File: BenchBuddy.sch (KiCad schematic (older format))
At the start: 0 parts

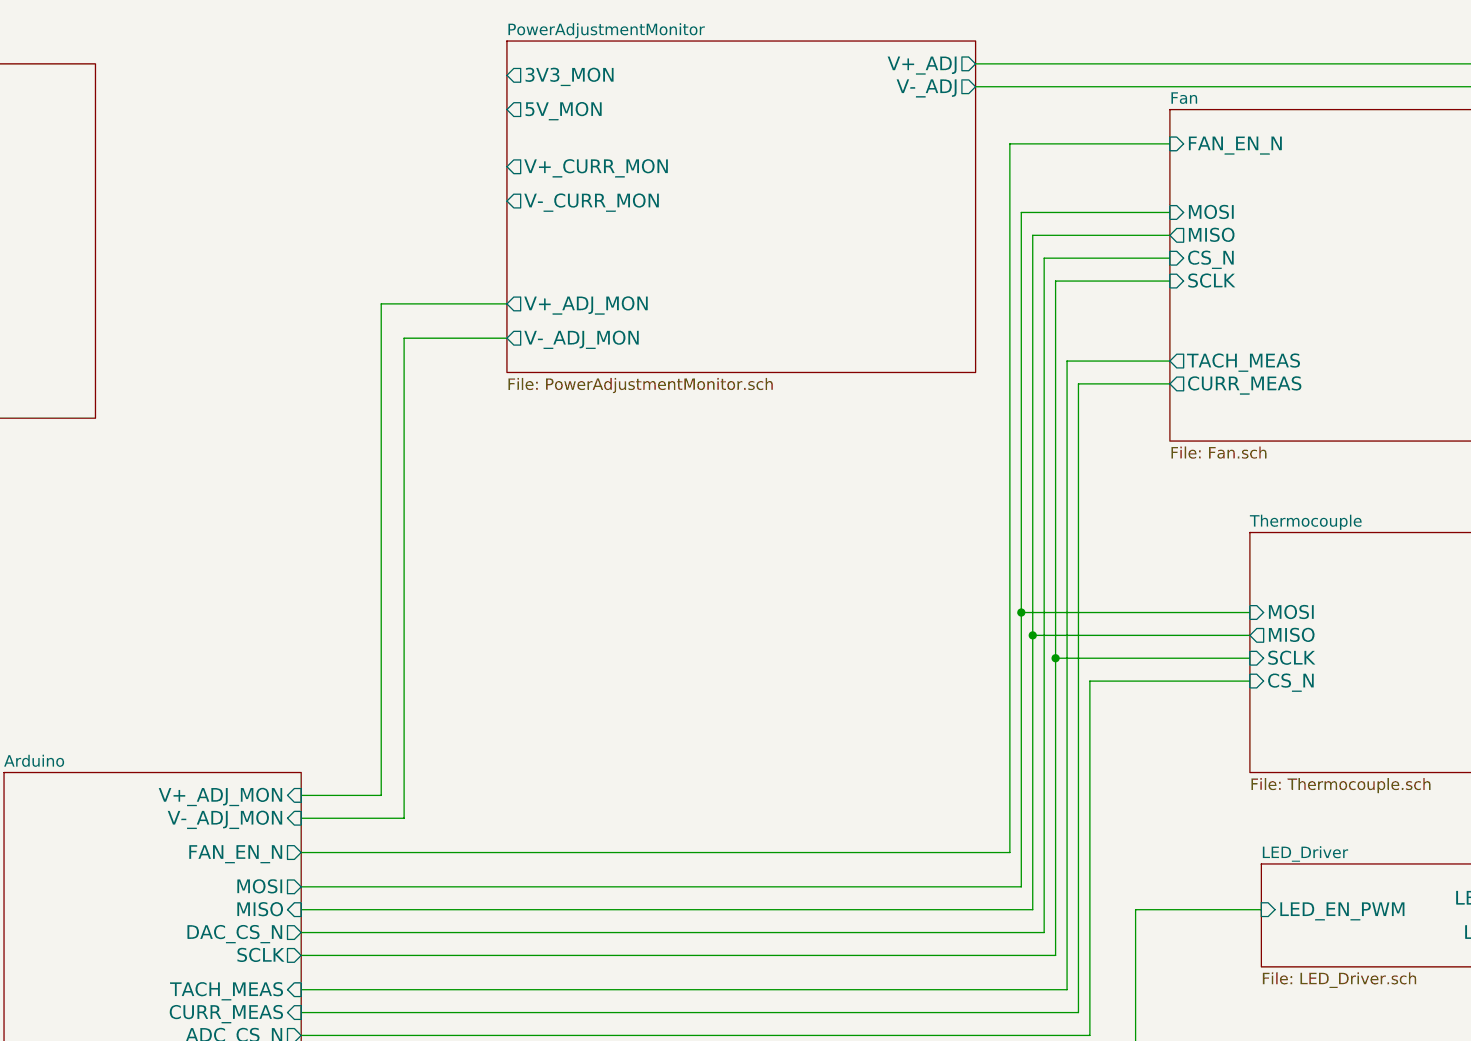
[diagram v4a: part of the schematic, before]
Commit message: Fan/Current Module Refactoring
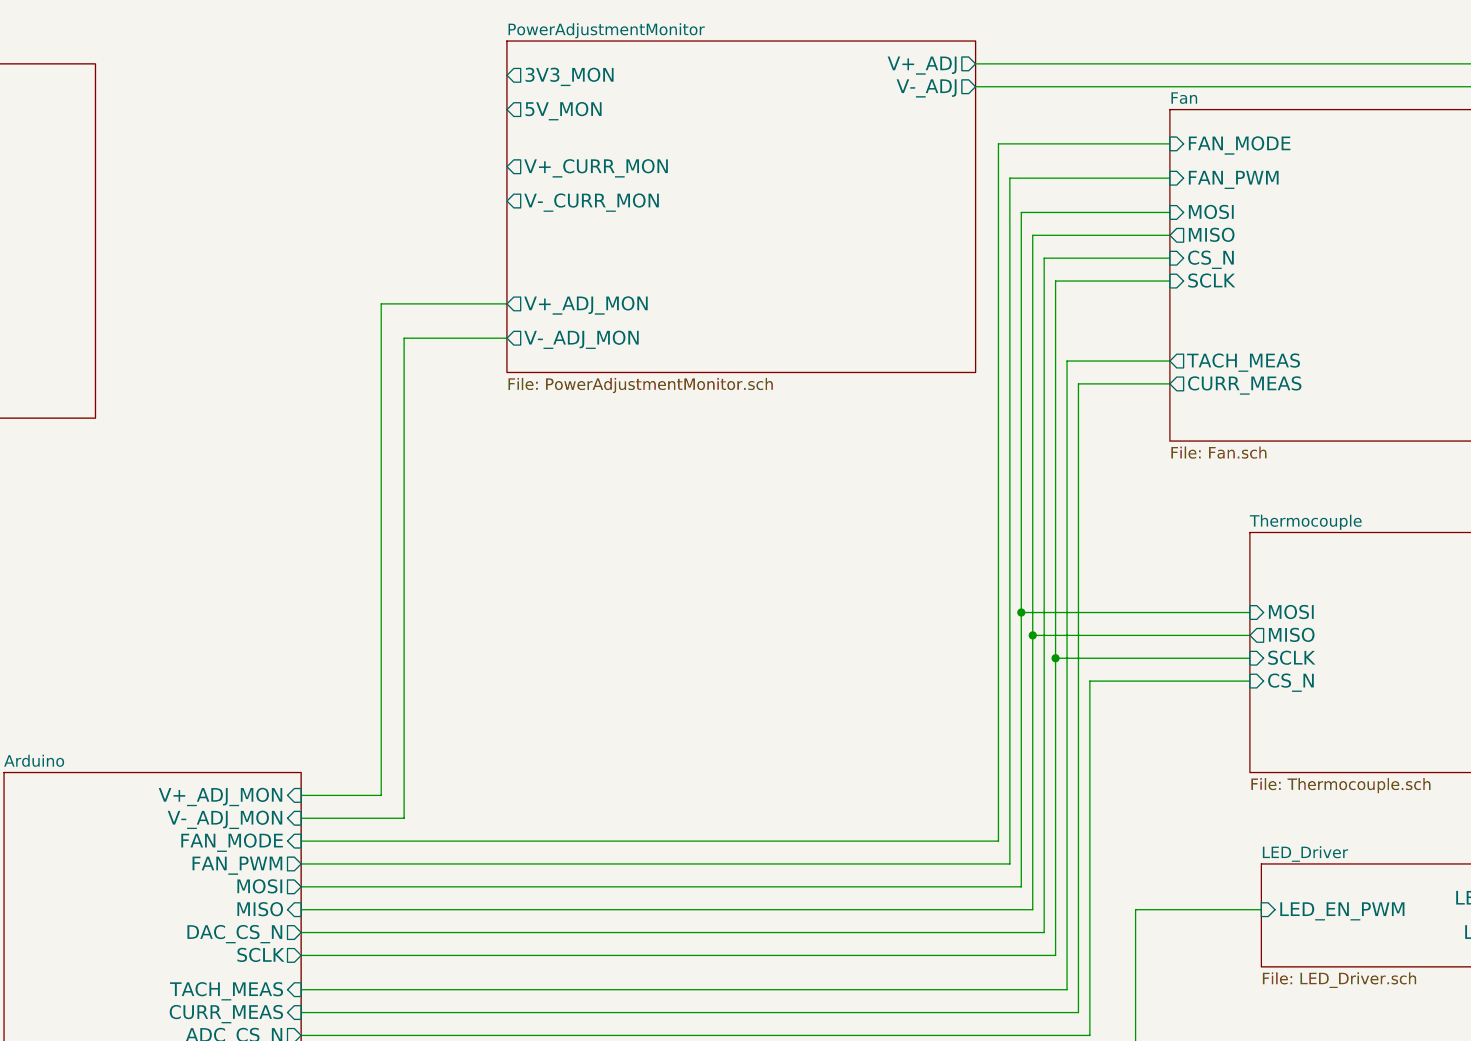
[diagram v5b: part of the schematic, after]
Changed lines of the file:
@@
 Sheet 1 9
 Title ""
-Date "28 sep 2013"
+Date "30 sep 2013"
 Rev ""
 Comp ""
@@
 F4 "CS_N" I L 7850 1750 60
 F5 "SCLK" I L 7850 1850 60
-F6 "FAN_EN_N" I L 7850 1250 60
-F7 "TACH_MEAS" O L 7850 2200 60
-F8 "FAN_OUT+" O R 9750 1350 60
-F9 "FAN_OUT-" O R 9750 1500 60
-F10 "TACH_IN" I R 9750 2300 60
-F11 "CURR_MEAS" O L 7850 2300 60
+F6 "TACH_MEAS" O L 7850 2200 60
+F7 "FAN_OUT+" O R 9750 1350 60
+F8 "FAN_OUT-" O R 9750 1500 60
+F9 "TACH_IN" I R 9750 2300 60
+F10 "CURR_MEAS" O L 7850 2300 60
+F11 "FAN_PWM" I L 7850 1400 60
+F12 "FAN_MODE" I L 7850 1250 60
 $EndSheet
 $Sheet
@@
 	4500 4200 4050 4200
 Wire Wire Line
-	4050 4350 7150 4350
-Wire Wire Line
-	7150 4350 7150 1250
-Wire Wire Line
-	7150 1250 7850 1250
-Wire Wire Line
 	7850 1550 7200 1550
 Wire Wire Line
@@
 F4 "MISO" I R 4050 4600 60
 F5 "SCLK" O R 4050 4800 60
-F6 "FAN_EN_N" O R 4050 4350 60
-F7 "CURR_MEAS" I R 4050 5050 60
-F8 "RELAY+" O R 4050 5800 60
-F9 "RELAY-" O R 4050 6000 60
-F10 "V+_ADJ_MON" I R 4050 4100 60
-F11 "V-_ADJ_MON" I R 4050 4200 60
-F12 "LED_EN_PWM" O R 4050 5300 60
-F13 "DAC_CS_N" O R 4050 4700 60
-F14 "ADC_CS_N" O R 4050 5150 60
+F6 "CURR_MEAS" I R 4050 5050 60
+F7 "RELAY+" O R 4050 5800 60
+F8 "RELAY-" O R 4050 6000 60
+F9 "V+_ADJ_MON" I R 4050 4100 60
+F10 "V-_ADJ_MON" I R 4050 4200 60
+F11 "LED_EN_PWM" O R 4050 5300 60
+F12 "DAC_CS_N" O R 4050 4700 60
+F13 "ADC_CS_N" O R 4050 5150 60
+F14 "FAN_PWM" O R 4050 4400 60
+F15 "FAN_MODE" I R 4050 4300 60
 $EndSheet
 Wire Wire Line
@@
 Wire Wire Line
 	9700 5900 10250 5900
+Wire Wire Line
+	7850 1400 7150 1400
+Wire Wire Line
+	7150 1400 7150 4400
+Wire Wire Line
+	7850 1250 7100 1250
+Wire Wire Line
+	7100 1250 7100 4300
+Wire Wire Line
+	7100 4300 4050 4300
+Wire Wire Line
+	7150 4400 4050 4400
 $EndSCHEMATC

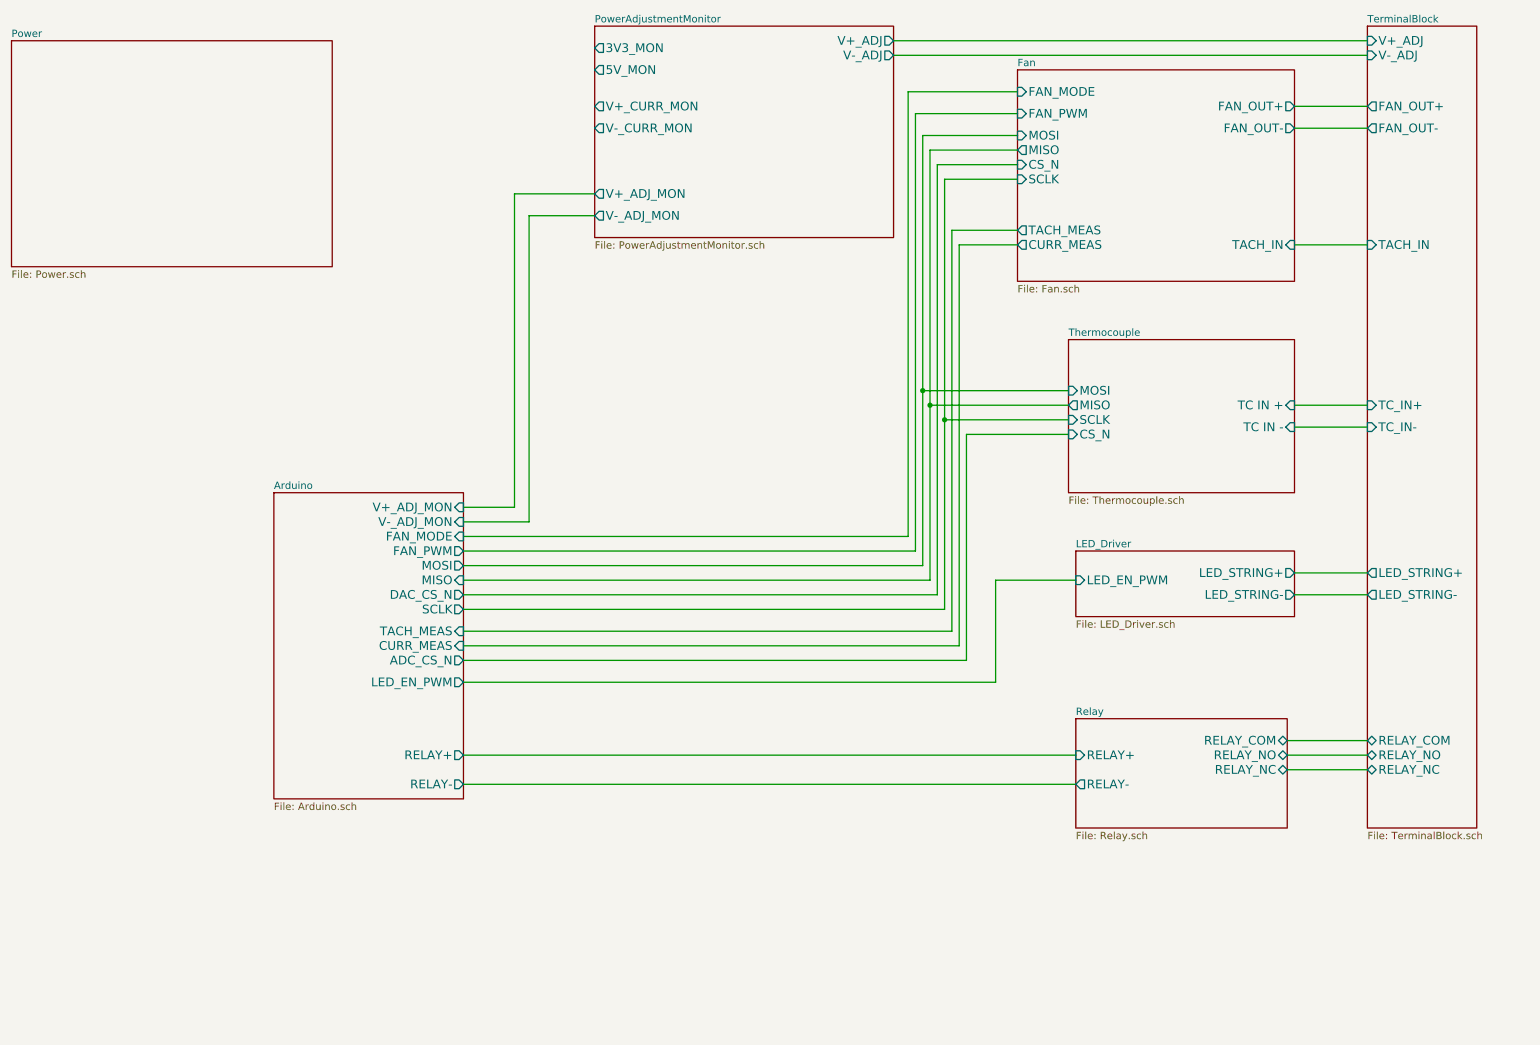
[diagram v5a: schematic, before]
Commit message: Preliminary Module Layouts
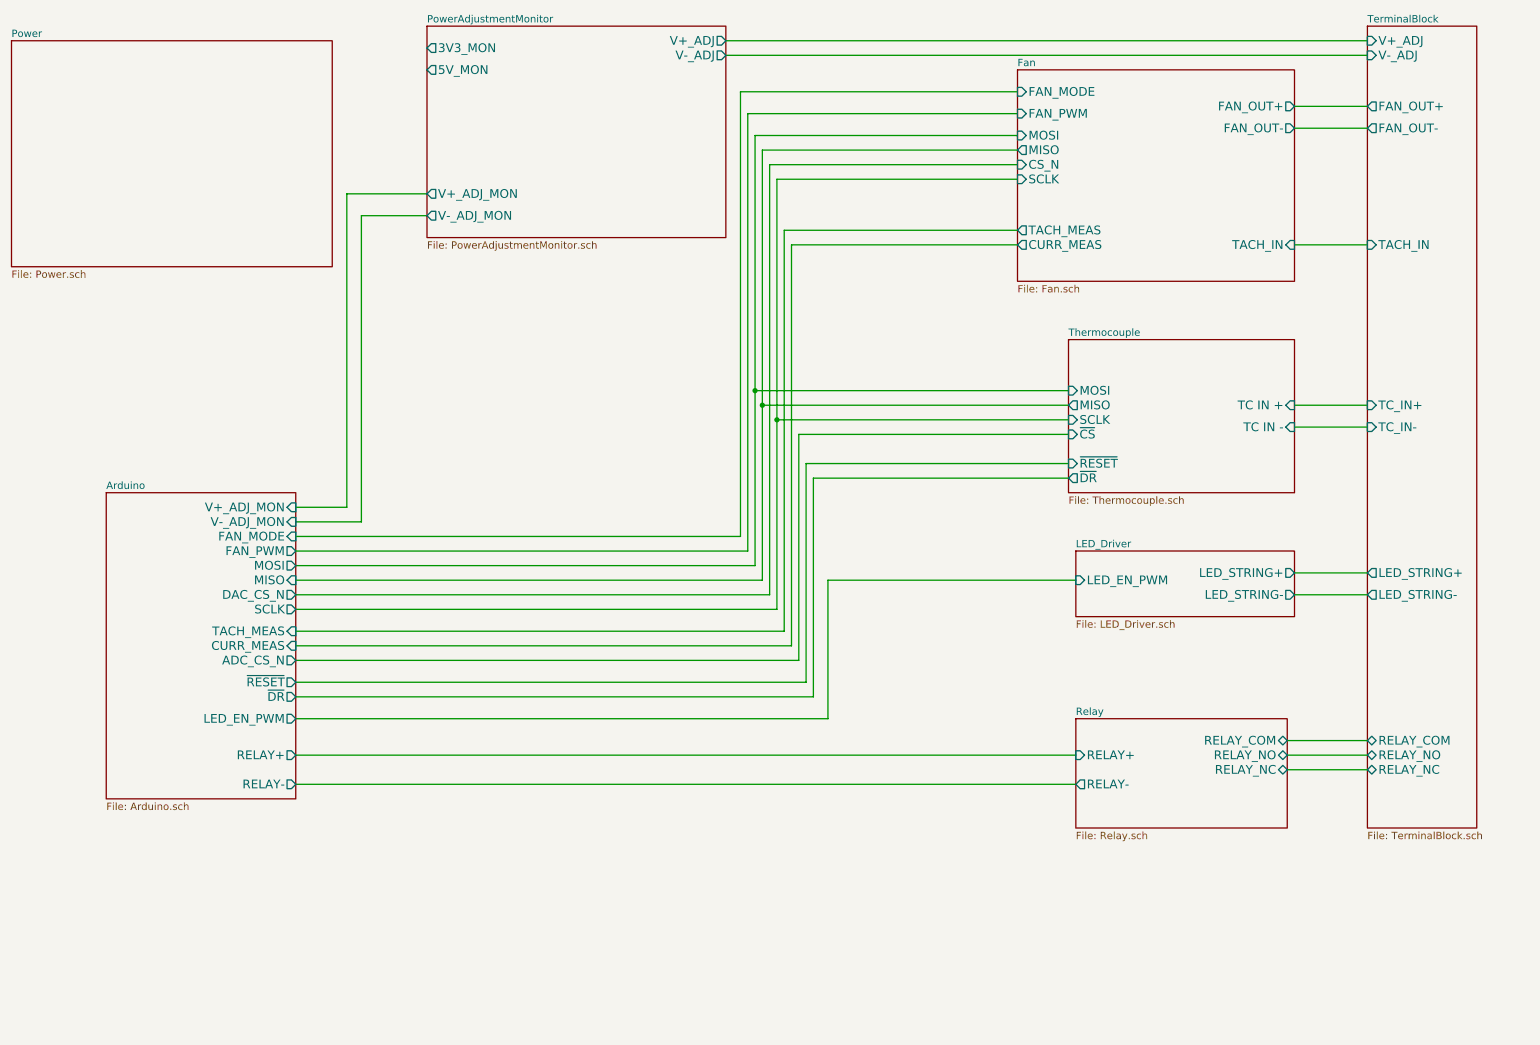
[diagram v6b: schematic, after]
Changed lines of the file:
@@
 Sheet 1 9
 Title ""
-Date "30 sep 2013"
+Date "15 oct 2013"
 Rev ""
 Comp ""
@@
 F5 "MISO" O L 8200 3400 60
 F6 "SCLK" I L 8200 3500 60
-F7 "CS_N" I L 8200 3600 60
+F7 "~CS" I L 8200 3600 60
+F8 "~DR" O L 8200 3900 60
+F9 "~RESET" I L 8200 3800 60
 $EndSheet
 $Sheet
@@
 $EndSheet
 $Sheet
-S 4950 800  2050 1450
+S 3800 800  2050 1450
 U 523E68DB
 F0 "PowerAdjustmentMonitor" 50
 F1 "PowerAdjustmentMonitor.sch" 50
-F2 "V+_ADJ" O R 7000 900 60
-F3 "V-_ADJ" O R 7000 1000 60
-F4 "3V3_MON" O L 4950 950 60
-F5 "5V_MON" O L 4950 1100 60
-F6 "V+_ADJ_MON" O L 4950 1950 60
-F7 "V-_ADJ_MON" O L 4950 2100 60
-F8 "V+_CURR_MON" O L 4950 1350 60
-F9 "V-_CURR_MON" O L 4950 1500 60
-$EndSheet
-Wire Wire Line
-	4050 4100 4400 4100
-Wire Wire Line
-	4400 4100 4400 1950
-Wire Wire Line
-	4400 1950 4950 1950
-Wire Wire Line
-	4950 2100 4500 2100
-Wire Wire Line
-	4500 2100 4500 4200
-Wire Wire Line
-	4500 4200 4050 4200
-Wire Wire Line
-	7850 1550 7200 1550
-Wire Wire Line
-	7200 1550 7200 4500
-Wire Wire Line
-	7200 4500 4050 4500
-Wire Wire Line
-	4050 4600 7250 4600
-Wire Wire Line
-	7250 4600 7250 1650
-Wire Wire Line
-	7250 1650 7850 1650
-Wire Wire Line
-	7850 1750 7300 1750
-Wire Wire Line
-	7300 1750 7300 4700
-Wire Wire Line
-	7300 4700 4050 4700
-Wire Wire Line
-	4050 4800 7350 4800
-Wire Wire Line
-	7350 4800 7350 1850
-Wire Wire Line
-	7350 1850 7850 1850
-Wire Wire Line
-	7850 2200 7400 2200
-Wire Wire Line
-	7400 2200 7400 4950
-Wire Wire Line
-	7400 4950 4050 4950
-Wire Wire Line
-	4050 5050 7450 5050
-Wire Wire Line
-	7450 5050 7450 2300
-Wire Wire Line
-	7450 2300 7850 2300
-Wire Wire Line
-	8200 3300 7200 3300
-Connection ~ 7200 3300
-Wire Wire Line
-	8200 3400 7250 3400
-Connection ~ 7250 3400
-$Sheet
-S 2750 4000 1300 2100
+F2 "V+_ADJ" O R 5850 900 60
+F3 "V-_ADJ" O R 5850 1000 60
+F4 "3V3_MON" O L 3800 950 60
+F5 "5V_MON" O L 3800 1100 60
+F6 "V+_ADJ_MON" O L 3800 1950 60
+F7 "V-_ADJ_MON" O L 3800 2100 60
+$EndSheet
+Wire Wire Line
+	2900 4100 3250 4100
+Wire Wire Line
+	3250 4100 3250 1950
+Wire Wire Line
+	3250 1950 3800 1950
+Wire Wire Line
+	3800 2100 3350 2100
+Wire Wire Line
+	3350 2100 3350 4200
+Wire Wire Line
+	3350 4200 2900 4200
+Wire Wire Line
+	7850 1550 6050 1550
+Wire Wire Line
+	6050 1550 6050 4500
+Wire Wire Line
+	6050 4500 2900 4500
+Wire Wire Line
+	6100 4600 2900 4600
+Wire Wire Line
+	6100 1650 6100 4600
+Wire Wire Line
+	6100 1650 7850 1650
+Wire Wire Line
+	7850 1750 6150 1750
+Wire Wire Line
+	6150 1750 6150 4700
+Wire Wire Line
+	6150 4700 2900 4700
+Wire Wire Line
+	6200 4800 2900 4800
+Wire Wire Line
+	6200 1850 6200 4800
+Wire Wire Line
+	6200 1850 7850 1850
+Wire Wire Line
+	7850 2200 6250 2200
+Wire Wire Line
+	6250 2200 6250 4950
+Wire Wire Line
+	6250 4950 2900 4950
+Wire Wire Line
+	2900 5050 6300 5050
+Wire Wire Line
+	6300 5050 6300 2300
+Wire Wire Line
+	6300 2300 7850 2300
+Wire Wire Line
+	8200 3300 6050 3300
+Connection ~ 6050 3300
+Wire Wire Line
+	8200 3400 6100 3400
+Connection ~ 6100 3400
+$Sheet
+S 1600 4000 1300 2100
 U 5237E014
 F0 "Arduino" 50
 F1 "Arduino.sch" 50
-F2 "TACH_MEAS" I R 4050 4950 60
-F3 "MOSI" O R 4050 4500 60
-F4 "MISO" I R 4050 4600 60
-F5 "SCLK" O R 4050 4800 60
-F6 "CURR_MEAS" I R 4050 5050 60
-F7 "RELAY+" O R 4050 5800 60
-F8 "RELAY-" O R 4050 6000 60
-F9 "V+_ADJ_MON" I R 4050 4100 60
-F10 "V-_ADJ_MON" I R 4050 4200 60
-F11 "LED_EN_PWM" O R 4050 5300 60
-F12 "DAC_CS_N" O R 4050 4700 60
-F13 "ADC_CS_N" O R 4050 5150 60
-F14 "FAN_PWM" O R 4050 4400 60
-F15 "FAN_MODE" I R 4050 4300 60
-$EndSheet
-Wire Wire Line
-	7350 3500 8200 3500
-Connection ~ 7350 3500
-Wire Wire Line
-	8200 3600 7500 3600
-Wire Wire Line
-	7500 3600 7500 5150
-Wire Wire Line
-	7500 5150 4050 5150
-Wire Wire Line
-	4050 5300 7700 5300
-Wire Wire Line
-	7700 5300 7700 4600
-Wire Wire Line
-	7700 4600 8250 4600
-Wire Wire Line
-	4050 5800 8250 5800
-Wire Wire Line
-	8250 6000 4050 6000
+F2 "TACH_MEAS" I R 2900 4950 60
+F3 "MOSI" O R 2900 4500 60
+F4 "MISO" I R 2900 4600 60
+F5 "SCLK" O R 2900 4800 60
+F6 "CURR_MEAS" I R 2900 5050 60
+F7 "RELAY+" O R 2900 5800 60
+F8 "RELAY-" O R 2900 6000 60
+F9 "V+_ADJ_MON" I R 2900 4100 60
+F10 "V-_ADJ_MON" I R 2900 4200 60
+F11 "LED_EN_PWM" O R 2900 5550 60
+F12 "DAC_CS_N" O R 2900 4700 60
+F13 "ADC_CS_N" O R 2900 5150 60
+F14 "FAN_PWM" O R 2900 4400 60
+F15 "FAN_MODE" I R 2900 4300 60
+F16 "~RESET" O R 2900 5300 60
+F17 "~DR" O R 2900 5400 60
+$EndSheet
+Wire Wire Line
+	6200 3500 8200 3500
+Connection ~ 6200 3500
+Wire Wire Line
+	8200 3600 6350 3600
+Wire Wire Line
+	6350 3600 6350 5150
+Wire Wire Line
+	6350 5150 2900 5150
+Wire Wire Line
+	2900 5550 6550 5550
+Wire Wire Line
+	6550 5550 6550 4600
+Wire Wire Line
+	6550 4600 8250 4600
+Wire Wire Line
+	2900 5800 8250 5800
+Wire Wire Line
+	8250 6000 2900 6000
 $Sheet
 S 10250 800  750  5500
@@
 $EndSheet
 Wire Wire Line
-	7000 900  10250 900
-Wire Wire Line
-	7000 1000 10250 1000
+	5850 900  10250 900
+Wire Wire Line
+	5850 1000 10250 1000
 Wire Wire Line
 	9750 1350 10250 1350
@@
 	9700 5900 10250 5900
 Wire Wire Line
-	7850 1400 7150 1400
-Wire Wire Line
-	7150 1400 7150 4400
-Wire Wire Line
-	7850 1250 7100 1250
-Wire Wire Line
-	7100 1250 7100 4300
-Wire Wire Line
-	7100 4300 4050 4300
-Wire Wire Line
-	7150 4400 4050 4400
+	7850 1400 6000 1400
+Wire Wire Line
+	6000 1400 6000 4400
+Wire Wire Line
+	7850 1250 5950 1250
+Wire Wire Line
+	5950 1250 5950 4300
+Wire Wire Line
+	5950 4300 2900 4300
+Wire Wire Line
+	6000 4400 2900 4400
+Wire Wire Line
+	2900 5300 6400 5300
+Wire Wire Line
+	6400 5300 6400 3800
+Wire Wire Line
+	6400 3800 8200 3800
+Wire Wire Line
+	8200 3900 6450 3900
+Wire Wire Line
+	6450 3900 6450 5400
+Wire Wire Line
+	6450 5400 2900 5400
 $EndSCHEMATC
